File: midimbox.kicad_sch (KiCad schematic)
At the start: 13 parts, among them J1 DIN-5, J2 DIN-5, J3 AudioJack3, J4 Conn_01x05, U1 6N138, U2 74LS00

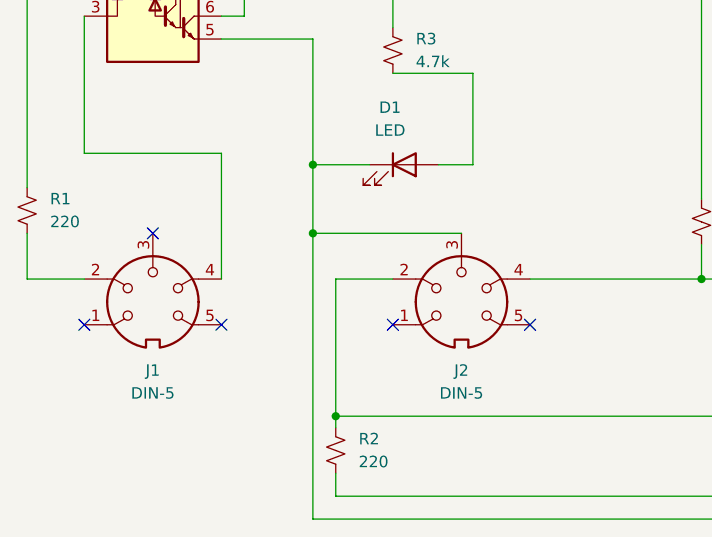
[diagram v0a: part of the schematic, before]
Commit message: Rough attempt at modelling the PCB.
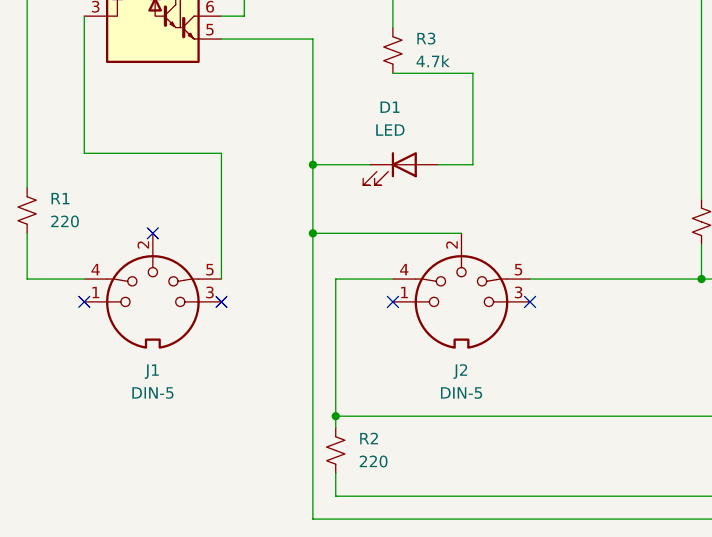
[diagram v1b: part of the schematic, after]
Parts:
- D1, D2: footprint LED_THT:LED_D10.0mm -> LED_THT:LED_D5.0mm
- J1, J2: footprint (none) -> AVConnectors:din-5; symbol Connector:DIN-5 -> Connector:DIN-5_180degree
- J3: footprint Connector_Audio:Jack_3.5mm_CUI_SJ-3523-SMT_Horizontal -> Connector_Audio:Jack_3.5mm_CUI_SJ1-3525N_Horizontal
- R1, R2, R3, R4, R5: footprint Resistor_SMD:R_0201_0603Metric -> Resistor_THT:R_Axial_DIN0204_L3.6mm_D1.6mm_P7.62mm_Horizontal
- U1: footprint Package_DIP:DIP-8-16_W7.62mm_Socket -> Package_DIP:DIP-8_W7.62mm_Socket
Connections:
- net at D1.1 (K), D2.1 (K), J3.S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: now also J2.2; no longer J2.3
- net at J3.R, R4.2: now also J2.5; no longer J2.4
- net at J3.T, R2.1: now also J2.4; no longer J2.2
- net at J1.2: no longer R1.2
- net at J1.4: now also R1.2; no longer U1.3 (C2)
- net at J1.5: now also U1.3 (C2)
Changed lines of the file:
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@@
   (junction (at 187.96 19.05) (diameter 0) (color 0 0 0 0)
   )
-  (no_connect (at 109.22 142.24))
-  (no_connect (at 93.98 142.24))
+  (no_connect (at 109.22 139.7))
+  (no_connect (at 93.98 139.7))
   (no_connect (at 175.26 62.23))
   (no_connect (at 74.93 102.87))
   (no_connect (at 67.31 132.08))
-  (no_connect (at 74.93 142.24))
-  (no_connect (at 59.69 142.24))
+  (no_connect (at 74.93 139.7))
+  (no_connect (at 59.69 139.7))
   (wire (pts (xy 93.98 137.16) (xy 87.63 137.16))
     (stroke (width 0) (type default) (color 0 0 0 0))
@@
     (property "Reference" "D1" (id 0) (at 93.6625 118.11 0))
     (property "Value" "LED" (id 1) (at 93.6625 120.65 0))
-    (property "Footprint" "LED_THT:LED_D10.0mm" (id 2) (at 95.25 124.46 0)
+    (property "Footprint" "LED_THT:LED_D5.0mm" (id 2) (at 95.25 124.46 0)
       (effects (font (size 1.27 1.27)) hide)
     )
@@
       (effects (font (size 1.27 1.27)) (justify left))
     )
-    (property "Footprint" "Resistor_SMD:R_0201_0603Metric" (id 2) (at 128.27 130.81 0)
+    (property "Footprint" "Resistor_THT:R_Axial_DIN0204_L3.6mm_D1.6mm_P7.62mm_Horizontal" (id 2) (at 128.27 130.81 0)
       (effects (font (size 1.27 1.27)) hide)
     )
@@
       (effects (font (size 1.27 1.27)) (justify right))
     )
-    (property "Footprint" "Connector_Audio:Jack_3.5mm_CUI_SJ-3523-SMT_Horizontal" (id 2) (at 173.99 123.19 0)
+    (property "Footprint" "Connector_Audio:Jack_3.5mm_CUI_SJ1-3525N_Horizontal" (id 2) (at 173.99 123.19 0)
       (effects (font (size 1.27 1.27)) hide)
     )
@@
     (pin "7")
   )
-  (symbol (lib_id "Connector:DIN-5") (at 67.31 139.7 0) (unit 1)
+  (symbol (lib_id "Connector:DIN-5_180degree") (at 67.31 139.7 0) (unit 1)
     (in_bom yes) (on_board yes) (fields_autoplaced)
     (property "Reference" "J1" (id 0) (at 67.3101 147.32 0))
     (property "Value" "DIN-5" (id 1) (at 67.3101 149.86 0))
-    (property "Footprint" "" (id 2) (at 67.31 139.7 0)
+    (property "Footprint" "AVConnectors:din-5" (id 2) (at 67.31 139.7 0)
       (effects (font (size 1.27 1.27)) hide)
     )
@@
       (effects (font (size 1.27 1.27)) (justify left))
     )
-    (property "Footprint" "Resistor_SMD:R_0201_0603Metric" (id 2) (at 53.34 129.54 0)
+    (property "Footprint" "Resistor_THT:R_Axial_DIN0204_L3.6mm_D1.6mm_P7.62mm_Horizontal" (id 2) (at 53.34 129.54 0)
       (effects (font (size 1.27 1.27)) hide)
     )
@@
       (effects (font (size 1.27 1.27)) (justify left))
     )
-    (property "Footprint" "Resistor_SMD:R_0201_0603Metric" (id 2) (at 93.98 111.76 0)
+    (property "Footprint" "Resistor_THT:R_Axial_DIN0204_L3.6mm_D1.6mm_P7.62mm_Horizontal" (id 2) (at 93.98 111.76 0)
       (effects (font (size 1.27 1.27)) hide)
     )
@@
     (pin "2")
   )
-  (symbol (lib_id "Connector:DIN-5") (at 101.6 139.7 0) (unit 1)
+  (symbol (lib_id "Connector:DIN-5_180degree") (at 101.6 139.7 0) (unit 1)
     (in_bom yes) (on_board yes) (fields_autoplaced)
     (property "Reference" "J2" (id 0) (at 101.6001 147.32 0))
     (property "Value" "DIN-5" (id 1) (at 101.6001 149.86 0))
-    (property "Footprint" "" (id 2) (at 101.6 139.7 0)
+    (property "Footprint" "AVConnectors:din-5" (id 2) (at 101.6 139.7 0)
       (effects (font (size 1.27 1.27)) hide)
     )
@@
     (property "Reference" "U1" (id 0) (at 67.31 92.71 0))
     (property "Value" "6N138" (id 1) (at 67.31 95.25 0))
-    (property "Footprint" "Package_DIP:DIP-8-16_W7.62mm_Socket" (id 2) (at 74.676 113.03 0)
+    (property "Footprint" "Package_DIP:DIP-8_W7.62mm_Socket" (id 2) (at 74.676 113.03 0)
       (effects (font (size 1.27 1.27)) hide)
     )
@@
     (property "Reference" "D2" (id 0) (at 198.4375 68.58 0))
     (property "Value" "LED" (id 1) (at 198.4375 71.12 0))
-    (property "Footprint" "LED_THT:LED_D10.0mm" (id 2) (at 196.85 74.93 0)
+    (property "Footprint" "LED_THT:LED_D5.0mm" (id 2) (at 196.85 74.93 0)
       (effects (font (size 1.27 1.27)) hide)
     )
@@
       (effects (font (size 1.27 1.27)) (justify left))
     )
-    (property "Footprint" "Resistor_SMD:R_0201_0603Metric" (id 2) (at 87.63 156.21 0)
+    (property "Footprint" "Resistor_THT:R_Axial_DIN0204_L3.6mm_D1.6mm_P7.62mm_Horizontal" (id 2) (at 87.63 156.21 0)
       (effects (font (size 1.27 1.27)) hide)
     )
@@
       (effects (font (size 1.27 1.27)) (justify left))
     )
-    (property "Footprint" "Resistor_SMD:R_0201_0603Metric" (id 2) (at 182.88 80.01 0)
+    (property "Footprint" "Resistor_THT:R_Axial_DIN0204_L3.6mm_D1.6mm_P7.62mm_Horizontal" (id 2) (at 182.88 80.01 0)
       (effects (font (size 1.27 1.27)) hide)
     )
@@
     )
     (path "/14db8b01-52ec-4c5c-b2b4-22f4ba7d62d0"
-      (reference "D1") (unit 1) (value "LED") (footprint "LED_THT:LED_D10.0mm")
+      (reference "D1") (unit 1) (value "LED") (footprint "LED_THT:LED_D5.0mm")
     )
     (path "/87191706-5e51-4e3b-a885-a1b77e84846d"
-      (reference "D2") (unit 1) (value "LED") (footprint "LED_THT:LED_D10.0mm")
+      (reference "D2") (unit 1) (value "LED") (footprint "LED_THT:LED_D5.0mm")
     )
     (path "/501845fb-0c0e-470c-b9bf-2aa76eaaecbd"
-      (reference "J1") (unit 1) (value "DIN-5") (footprint "")
+      (reference "J1") (unit 1) (value "DIN-5") (footprint "AVConnectors:din-5")
     )
     (path "/5c8d5ef6-45c1-417e-b228-5a9c1e2108b6"
-      (reference "J2") (unit 1) (value "DIN-5") (footprint "")
+      (reference "J2") (unit 1) (value "DIN-5") (footprint "AVConnectors:din-5")
     )
     (path "/346a563f-a2ec-43ce-a871-e8915cc9ce99"
-      (reference "J3") (unit 1) (value "AudioJack3") (footprint "Connector_Audio:Jack_3.5mm_CUI_SJ-3523-SMT_Horizontal")
+      (reference "J3") (unit 1) (value "AudioJack3") (footprint "Connector_Audio:Jack_3.5mm_CUI_SJ1-3525N_Horizontal")
     )
     (path "/70169f0b-b499-438d-aa3c-eeabf5996457"
@@
     )
     (path "/57d1b540-ceb5-4504-a445-83774ed331b3"
-      (reference "R1") (unit 1) (value "220") (footprint "Resistor_SMD:R_0201_0603Metric")
+      (reference "R1") (unit 1) (value "220") (footprint "Resistor_THT:R_Axial_DIN0204_L3.6mm_D1.6mm_P7.62mm_Horizontal")
     )
     (path "/9a05b47a-7751-4dd6-8b23-70037f4614c3"
-      (reference "R2") (unit 1) (value "220") (footprint "Resistor_SMD:R_0201_0603Metric")
+      (reference "R2") (unit 1) (value "220") (footprint "Resistor_THT:R_Axial_DIN0204_L3.6mm_D1.6mm_P7.62mm_Horizontal")
     )
     (path "/5c0b3b28-e906-436d-8cbd-24b59764d4b0"
-      (reference "R3") (unit 1) (value "4.7k") (footprint "Resistor_SMD:R_0201_0603Metric")
+      (reference "R3") (unit 1) (value "4.7k") (footprint "Resistor_THT:R_Axial_DIN0204_L3.6mm_D1.6mm_P7.62mm_Horizontal")
     )
     (path "/21b7823f-79b3-4af1-bc7c-6978160f801f"
-      (reference "R4") (unit 1) (value "220") (footprint "Resistor_SMD:R_0201_0603Metric")
+      (reference "R4") (unit 1) (value "220") (footprint "Resistor_THT:R_Axial_DIN0204_L3.6mm_D1.6mm_P7.62mm_Horizontal")
     )
     (path "/9eefc540-4038-4653-af9d-f2ee5e9a4ee5"
-      (reference "R5") (unit 1) (value "4.7k") (footprint "Resistor_SMD:R_0201_0603Metric")
+      (reference "R5") (unit 1) (value "4.7k") (footprint "Resistor_THT:R_Axial_DIN0204_L3.6mm_D1.6mm_P7.62mm_Horizontal")
     )
     (path "/6eb3adfc-a10d-4b97-848d-d6b6771d8aa0"
-      (reference "U1") (unit 1) (value "6N138") (footprint "Package_DIP:DIP-8-16_W7.62mm_Socket")
+      (reference "U1") (unit 1) (value "6N138") (footprint "Package_DIP:DIP-8_W7.62mm_Socket")
     )
     (path "/6910cc22-d6f7-4b13-bb49-12bf79f8b36a"
